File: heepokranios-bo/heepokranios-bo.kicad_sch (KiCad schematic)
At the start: 122 parts, among them J1 Conn_02x02_Odd_Even, J11 PGA_13x13, J14 Conn_02x03_Odd_Even, J15 Conn_02x08_Odd_Even, J16 Conn_02x03_Odd_Even, J17 Conn_02x03_Odd_Even, J2 Conn_02x02_Odd_Even, J3 Conn_02x03_Odd_Even, J4 Conn_02x03_Odd_Even, J5 Conn_02x03_Odd_Even, J6 Conn_02x04_Odd_Even, J8 Conn_02x03_Odd_Even, J9 Conn_02x02_Odd_Even, SW1 SW_Push

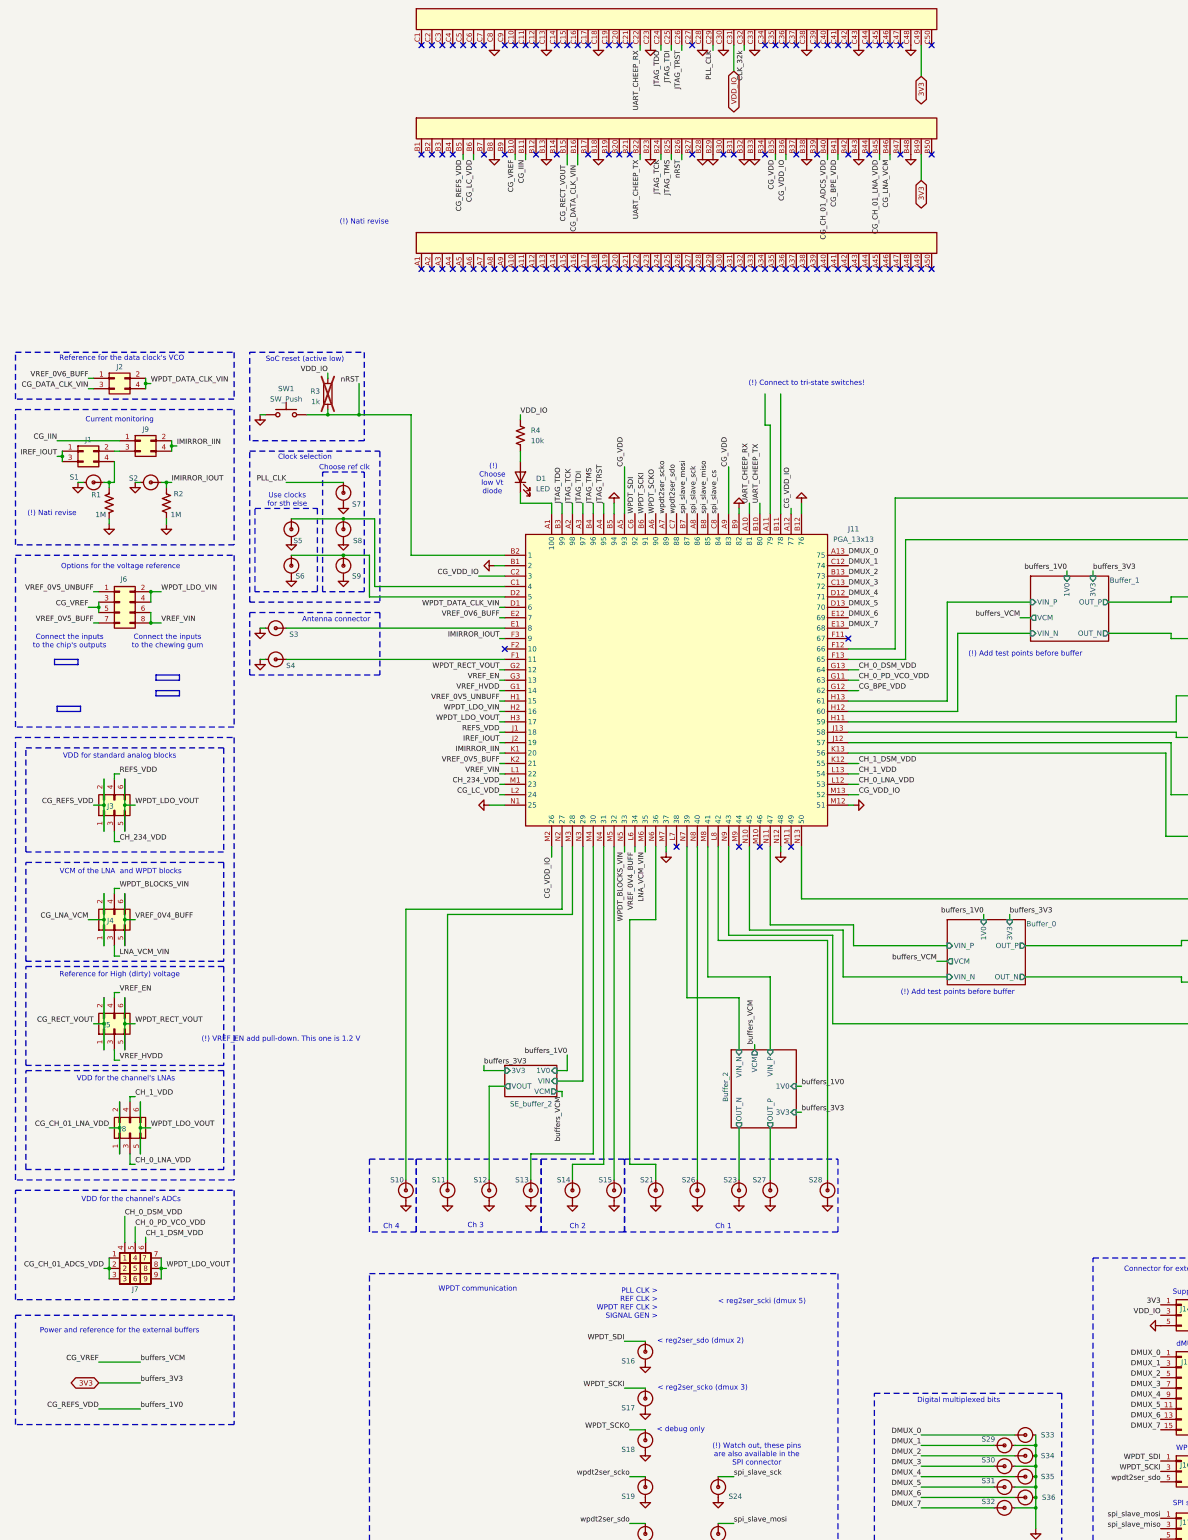
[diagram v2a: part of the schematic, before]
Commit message: Cheep connector (connections to main board): revised, modified 3V3 pin and added references to their values. Also modified the circuit to the current pins (resistor values + new pin headers)
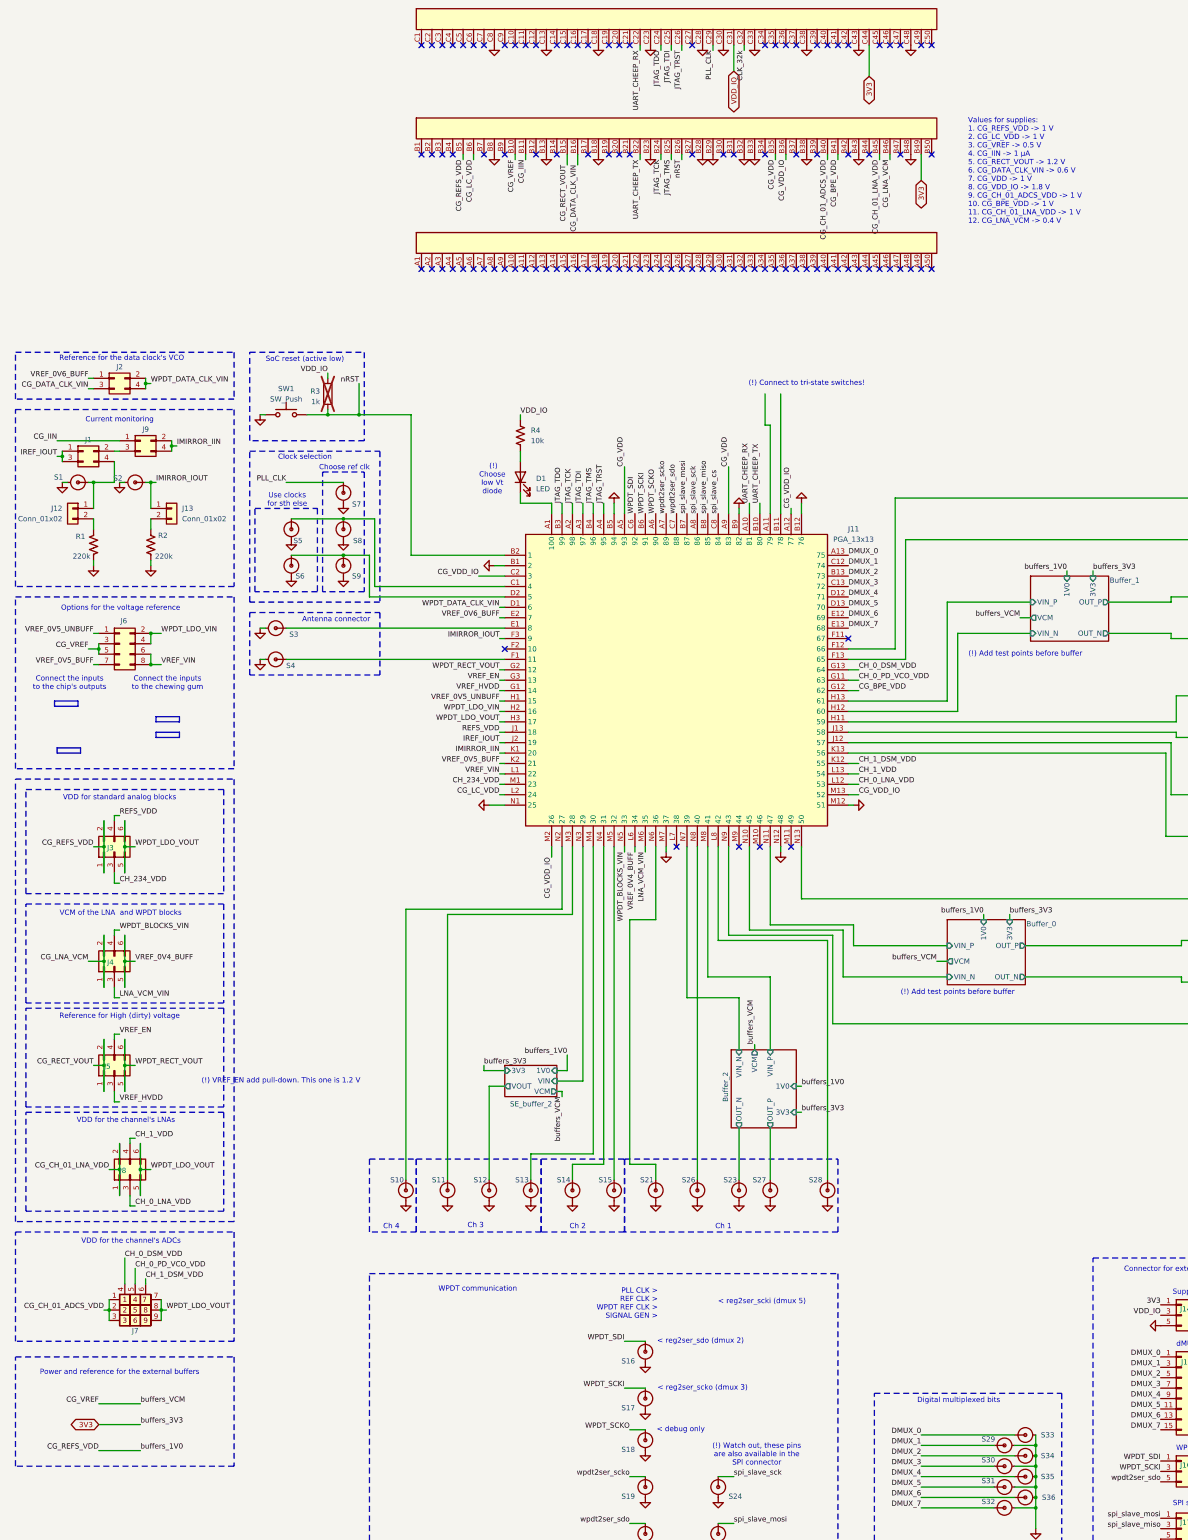
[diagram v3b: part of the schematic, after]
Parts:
- added J12, J13: Conn_01x02, Connector_PinHeader_2.54mm:PinHeader_1x02_P2.54mm_Vertical, symbol Connector_Generic:Conn_01x02
- R1, R2: value 1M -> 220k
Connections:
- net 3V3: now also J10.C44; no longer J10.C49
- net IMIRROR_IOUT: now also J13.1 (Pin_1); no longer R2.1
- net at J1.4 (Pin_4), S1.1: now also J12.1 (Pin_1); no longer R1.1
- new net: J13.2 (Pin_2), R2.1
- new net: J12.2 (Pin_2), R1.1
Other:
- note added: "Values for supplies: 1. CG_REFS_VDD -> 1 V 2. CG_LC_VDD -> 1 V 3. CG_VREF -> 0.5 V 4. CG_IIN -> 1 μA 5. CG_RECT_VOUT -> 1.2 V 6. CG_DATA_CLK_VIN -> 0.6 V 7. CG_VDD -> 1 V 8. CG_VDD_IO -> 1.8 V 9. CG_CH_01_ADCS_VDD -> 1 V 10. CG_BPE_VDD -> 1 V 11. CG_CH_01_LNA_VDD -> 1 V 12. CG_LNA_VCM -> 0.4 V"
- note removed: "(!) Nati revise"
- moved on the sheet: J3, J4, J5, J6, J7, J8, R1, R2, S1, S2
